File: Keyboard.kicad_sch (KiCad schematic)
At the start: 39 parts, among them J1 USB_C_Receptacle, J2 Conn_02x01, J4 FFC2B35-16-G_REVA2, Q1 PMOS, Q2 NMOS, Q3 NMOS, U1 VBUS54CV-HSF-G4-08, U3 MCP73831-2-OT, U4 LM1117DT-3.3, U5 ESP32-S3-WROOM-1-N16R2

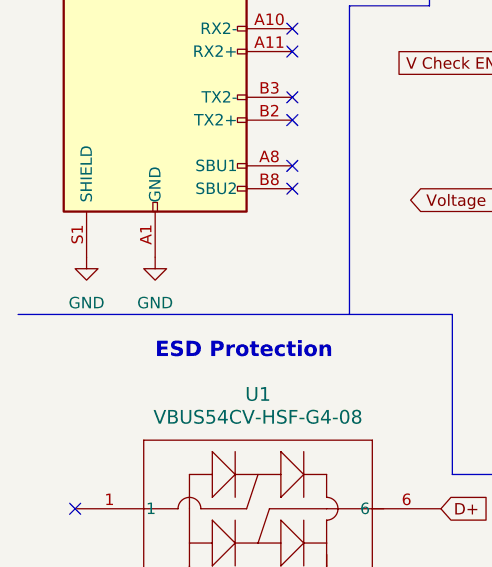
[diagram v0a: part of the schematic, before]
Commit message: basically finished wiring, now just need to add reset button and video wire hole
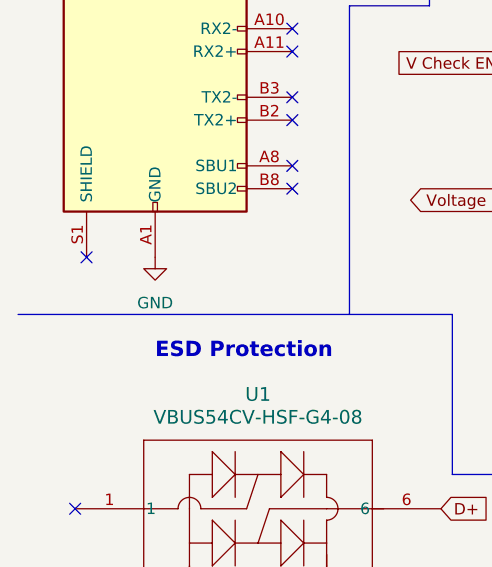
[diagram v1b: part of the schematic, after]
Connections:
- net GND: no longer J1.S1 (SHIELD)
- no-connect marks 12 -> 13
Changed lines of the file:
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@@
   (no_connect (at 43.18 62.23))
   (no_connect (at 43.18 64.77))
+  (no_connect (at 20.32 95.25))
   (no_connect (at 43.18 57.15))
   (no_connect (at 43.18 54.61))
@@
         )
       )
-    )
-  )
-  (symbol (lib_id "power:GND") (at 20.32 95.25 0) (unit 1)
-    (in_bom yes) (on_board yes) (dnp no) (fields_autoplaced)
-    (property "Reference" "#PWR07" (at 20.32 101.6 0)
-      (effects (font (size 1.27 1.27)) hide)
-    )
-    (property "Value" "GND" (at 20.32 100.33 0)
-      (effects (font (size 1.27 1.27)))
-    )
-    (property "Footprint" "" (at 20.32 95.25 0)
-      (effects (font (size 1.27 1.27)) hide)
-    )
-    (property "Datasheet" "" (at 20.32 95.25 0)
-      (effects (font (size 1.27 1.27)) hide)
-    )
-    (pin "1")
-    (instances
-      (project "Keyboard"
-        (path "/0c6e22c2-b00a-47ce-bc43-0c577bef5c57"
-          (reference "#PWR07") (unit 1)
-        )
-      )

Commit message: finished pcb
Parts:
- added R16: 5.1k ohm, Resistor_SMD:R_0402_1005Metric, symbol Device:R
- added SW1: SW_MEC_5G, Button_Switch_SMD:SW_MEC_5GSH9, symbol Switch:SW_MEC_5G
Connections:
- net GND: now also SW1.1 (A), SW1.2 (A)
- net at C1.2, R9.2, U5.3 (EN): now also R16.2
- new net: R16.1, SW1.3 (B), SW1.4 (B)
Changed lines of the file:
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@@
   (junction (at 149.86 29.21) (diameter 0) (color 0 0 0 0)
+  )
+  (junction (at 104.14 29.21) (diameter 0) (color 0 0 0 0)
   )
   (junction (at 73.66 88.9) (diameter 0) (color 0 0 0 0)
@@
     (stroke (width 0) (type default))
   )
-  (wire (pts (xy 104.14 26.67) (xy 104.14 31.75))
+  (wire (pts (xy 104.14 26.67) (xy 104.14 29.21))
     (stroke (width 0) (type default))
   )
@@
     (stroke (width 0) (type default))
   )
+  (wire (pts (xy 90.17 26.67) (xy 93.98 26.67))
+    (stroke (width 0) (type default))
+  )
   (wire (pts (xy 102.87 142.24) (xy 105.41 142.24))
     (stroke (width 0) (type default))
@@
     (stroke (width 0) (type default))
   )
+  (wire (pts (xy 66.04 33.02) (xy 66.04 29.21))
+    (stroke (width 0) (type default))
+  )
   (wire (pts (xy 201.93 72.39) (xy 190.5 72.39))
     (stroke (width 0) (type default))
@@
     (stroke (width 0) (type default))
   )
+  (wire (pts (xy 104.14 29.21) (xy 104.14 31.75))
+    (stroke (width 0) (type default))
+  )
   (wire (pts (xy 44.45 46.99) (xy 44.45 48.26))
     (stroke (width 0) (type default))
@@
   )
   (wire (pts (xy 208.28 77.47) (xy 201.93 77.47))
+    (stroke (width 0) (type default))
+  )
+  (wire (pts (xy 104.14 29.21) (xy 83.82 29.21))
     (stroke (width 0) (type default))
   )
@@
     )
   )
-  (global_label "EN In" (shape input) (at 93.98 26.67 180) (fields_autoplaced)
-    (effects (font (size 1.27 1.27)) (justify right))
-    (property "Intersheetrefs" "${INTERSHEET_REFS}" (at 85.7939 26.67 0)
-      (effects (font (size 1.27 1.27)) (justify right) hide)
+  (global_label "EN In" (shape input) (at 90.17 26.67 90) (fields_autoplaced)
+    (effects (font (size 1.27 1.27)) (justify left))
+    (property "Intersheetrefs" "${INTERSHEET_REFS}" (at 90.17 18.4839 90)
+      (effects (font (size 1.27 1.27)) (justify left) hide)
     )
   )
@@
   )
   (symbol (lib_id "power:GND") (at 91.44 31.75 0) (unit 1)
-    (in_bom yes) (on_board yes) (dnp no) (fields_autoplaced)
+    (in_bom yes) (on_board yes) (dnp no)
     (property "Reference" "#PWR019" (at 91.44 38.1 0)
       (effects (font (size 1.27 1.27)) hide)
     )
-    (property "Value" "GND" (at 91.44 36.83 0)
+    (property "Value" "GND" (at 88.9 31.75 0)
       (effects (font (size 1.27 1.27)))
     )
@@
     )
   )
+  (symbol (lib_id "Device:R") (at 80.01 29.21 90) (unit 1)
+    (in_bom yes) (on_board yes) (dnp no)
+    (property "Reference" "R16" (at 77.47 24.13 90)
+      (effects (font (size 1.27 1.27)) (justify right))
+    )
+    (property "Value" "5.1k ohm" (at 77.47 26.67 90)
+      (effects (font (size 1.27 1.27)) (justify right))
+    )
+    (property "Footprint" "Resistor_SMD:R_0402_1005Metric" (at 80.01 30.988 90)
+      (effects (font (size 1.27 1.27)) hide)
+    )
+    (property "Datasheet" "~" (at 80.01 29.21 0)
+      (effects (font (size 1.27 1.27)) hide)
+    )
+    (pin "1")
+    (pin "2")
+    (instances
+      (project "Keyboard"
+        (path "/0c6e22c2-b00a-47ce-bc43-0c577bef5c57"
+          (reference "R16") (unit 1)
+        )
+      )
+    )
+  )
   (symbol (lib_id "Device:R") (at 187.96 92.71 90) (unit 1)
     (in_bom yes) (on_board yes) (dnp no)
@@
     )
   )
+  (symbol (lib_id "Switch:SW_MEC_5G") (at 71.12 29.21 0) (unit 1)
+    (in_bom yes) (on_board yes) (dnp no) (fields_autoplaced)
+    (property "Reference" "SW1" (at 71.12 21.59 0)
+      (effects (font (size 1.27 1.27)))
+    )
+    (property "Value" "SW_MEC_5G" (at 71.12 24.13 0)
+      (effects (font (size 1.27 1.27)))
+    )
+    (property "Footprint" "Button_Switch_SMD:SW_MEC_5GSH9" (at 71.12 24.13 0)
+      (effects (font (size 1.27 1.27)) hide)
+    )
+    (property "Datasheet" "http://www.apem.com/int/index.php?controller=attachment&id_attachment=488" (at 71.12 24.13 0)
+      (effects (font (size 1.27 1.27)) hide)
+    )
+    (pin "1")
+    (pin "3")
+    (pin "2")
+    (pin "4")
+    (instances
+      (project "Keyboard"
+        (path "/0c6e22c2-b00a-47ce-bc43-0c577bef5c57"
+          (reference "SW1") (unit 1)
+        )
+      )
+    )
+  )
   (symbol (lib_id "Device:R") (at 147.32 115.57 0) (unit 1)
     (in_bom yes) (on_board yes) (dnp no)
@@
         )
       )
+    )
+  )
+  (symbol (lib_id "power:GND") (at 66.04 33.02 0) (unit 1)
+    (in_bom yes) (on_board yes) (dnp no) (fields_autoplaced)
+    (property "Reference" "#PWR07" (at 66.04 39.37 0)
+      (effects (font (size 1.27 1.27)) hide)
+    )
+    (property "Value" "GND" (at 66.04 38.1 0)
+      (effects (font (size 1.27 1.27)))
+    )
+    (property "Footprint" "" (at 66.04 33.02 0)
+      (effects (font (size 1.27 1.27)) hide)
+    )
+    (property "Datasheet" "" (at 66.04 33.02 0)
+      (effects (font (size 1.27 1.27)) hide)
+    )
+    (pin "1")
+    (instances
+      (project "Keyboard"
+        (path "/0c6e22c2-b00a-47ce-bc43-0c577bef5c57"
+          (reference "#PWR07") (unit 1)
+        )
+      )
